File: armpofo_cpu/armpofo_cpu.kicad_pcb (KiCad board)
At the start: 2 copper layers, 185.1 x 74 mm, 94 parts, among them J1 USB_OTG, J10 Conn_01x16, J11 Conn_01x20, J2 Conn_01x01, J3 Conn_01x01, J4 Conn_01x16, J5 Conn_01x20, J6 Conn_02x16_Odd_Even, J7 Conn_01x08, J8 Micro_SD_Card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

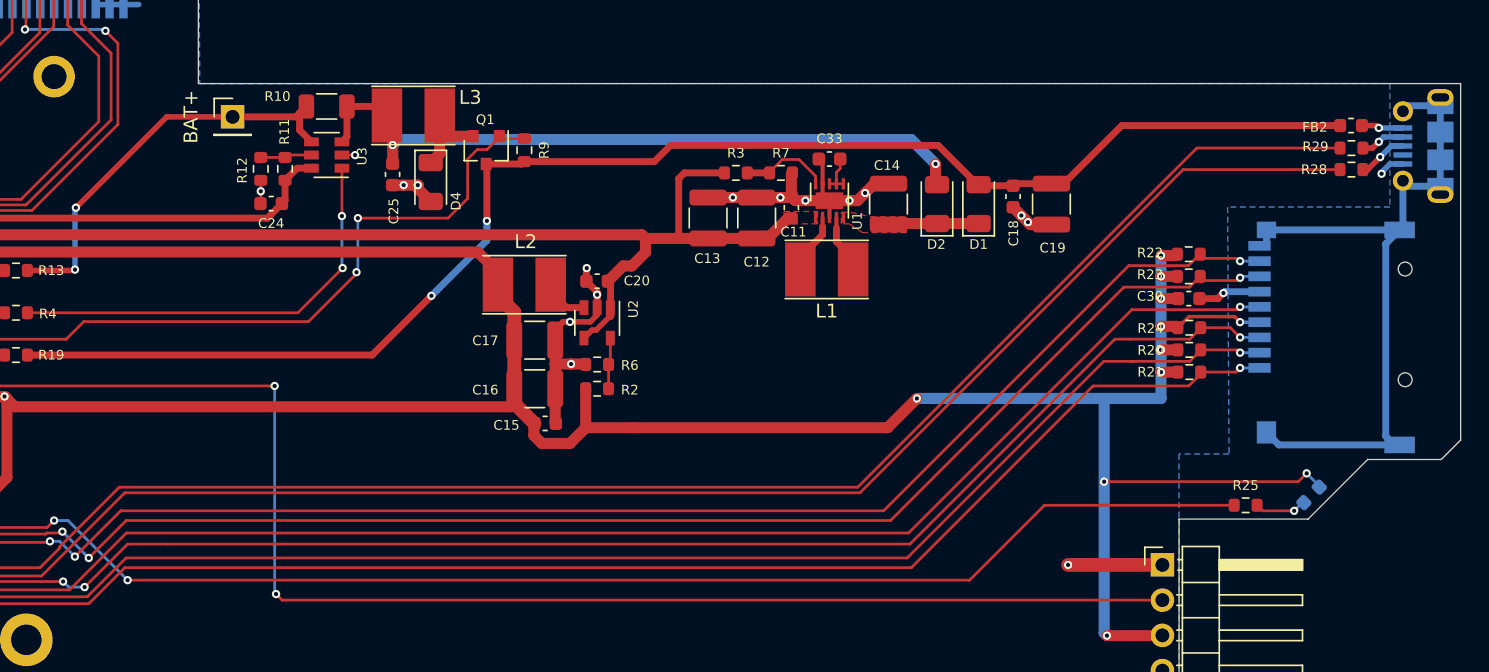
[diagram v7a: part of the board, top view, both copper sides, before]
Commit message: usb overstrecht corrected
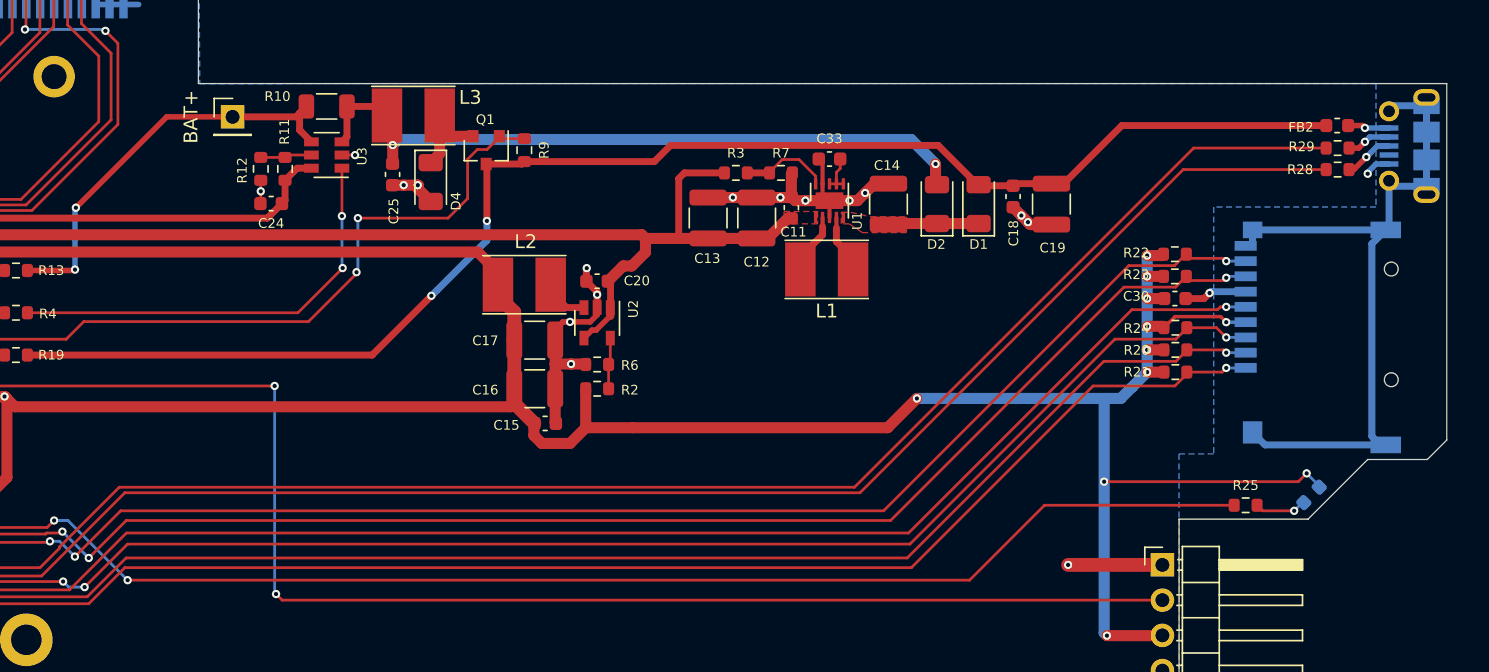
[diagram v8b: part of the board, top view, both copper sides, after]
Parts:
- moved C30 1.00 mm to (232.9, 102.1)
- moved FB2 1.00 mm to (244.6, 89.6)
- moved J1 1.00 mm to (249.8, 91.1)
- moved J8 1.00 mm to (248.5, 104.9)
- moved R20 1.00 mm to (232.9, 105.8)
- moved R21 1.00 mm to (232.9, 107.4)
- moved R22 1.00 mm to (232.9, 98.9)
- moved R23 1.00 mm to (232.9, 100.5)
- moved R24 1.00 mm to (232.9, 104.2)
- moved R28 1.00 mm to (244.6, 92.8)
- moved R29 1.00 mm to (244.6, 91.2)
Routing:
- net +3V3: track 445.1 -> 443.0 mm
- net /SDCARD-D3: track 141.5 -> 140.4 mm
- net /USB5V: track 107.9 -> 106.9 mm
- net /USB-DP: track 150.6 -> 149.6 mm
- net /SDCARD-D2: track 142.0 -> 141.0 mm
- net /SDCARD-D1: track 142.3 -> 141.3 mm
- net /SDCARD-CMD: track 138.6 -> 137.6 mm
- net /USB-DM: track 151.2 -> 150.2 mm
- net /SDCARD-D0: track 142.3 -> 141.3 mm
- net /SDCARD-CK: track 141.5 -> 140.5 mm
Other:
- board size 185.1 x 74 mm -> 184.1 x 74 mm
